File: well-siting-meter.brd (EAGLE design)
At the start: 93.8 x 65.9 mm, 55 parts, among them IC1 LM336LP, J2 7805, T1 MOSFET-NCHANNELFQP30N06L, U1 LCD-16X2NOHOLES, U2 ARDUINO_PRO_MINI, U3 EC2, U4 EC2, U5 AD623, U6 AD629, U7 MAX1771

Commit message: rev B build
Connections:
- net RSW: now also U2.10; no longer U2.A5
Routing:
- net RSW: track 33.9 -> 54.7 mm
- net VO: track 40.7 -> 40.1 mm
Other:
- board text added: "danwahl.net/"
- board text removed: "danwahl.github.io/"
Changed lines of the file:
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@@
 <text x="92.71" y="42.418" size="1.4224" layer="121" font="vector" ratio="10" rot="R90">well-siting-meter</text>
 <text x="87.63" y="40.64" size="0.8128" layer="121" font="vector" ratio="10" rot="R90">v2</text>
-<text x="92.71" y="30.48" size="0.8128" layer="121" font="vector" ratio="10" rot="R90">danwahl.github.io/</text>
+<text x="92.71" y="34.29" size="0.8128" layer="121" font="vector" ratio="10" rot="R90">danwahl.net/</text>
 <text x="87.63" y="64.77" size="1.016" layer="121" font="vector" ratio="10" align="center">BATT</text>
 <text x="71.374" y="64.77" size="1.016" layer="121" font="vector" ratio="10" align="center">GND</text>
@@
 </element>
 <element name="C1" library="SparkFun-Passives" package="CPOL-RADIAL-1000UF-25V" value="100uF" x="59.69" y="26.67" smashed="yes" rot="R180">
-<attribute name="NAME" x="60.452" y="25.019" size="0.8128" layer="25" font="vector" rot="R180"/>
+<attribute name="NAME" x="65.532" y="31.369" size="0.8128" layer="25" font="vector" rot="R180"/>
 <attribute name="PN" value="1572-1306-ND" x="59.69" y="26.67" size="1.778" layer="27" rot="R180" display="off"/>
 <attribute name="VALUE" x="62.357" y="29.972" size="0.8128" layer="27" font="vector" rot="R180"/>
@@
 <attribute name="NAME" x="48.26" y="22.098" size="0.8128" layer="25" font="vector" rot="R90"/>
 <attribute name="PN" value="BC2665CT-ND" x="49.53" y="24.13" size="1.778" layer="27" rot="R90" display="off"/>
-<attribute name="VALUE" x="51.562" y="20.574" size="0.8128" layer="27" font="vector" rot="R90"/>
+<attribute name="VALUE" x="51.562" y="24.384" size="0.8128" layer="27" font="vector" rot="R90"/>
 </element>
 <element name="C3" library="SparkFun-Passives" package="CAP-PTH-5MM" value="0.1uf" x="41.91" y="13.97" smashed="yes" rot="R180">
-<attribute name="NAME" x="40.132" y="12.7" size="0.8128" layer="25" font="vector" rot="R180"/>
+<attribute name="NAME" x="43.942" y="16.002" size="0.8128" layer="25" font="vector" rot="R180"/>
 <attribute name="PN" value="BC2665CT-ND" x="41.91" y="13.97" size="1.778" layer="27" rot="R180" display="off"/>
 <attribute name="VALUE" x="40.386" y="16.002" size="0.8128" layer="27" font="vector" rot="R180"/>
@@
 </element>
 <element name="R9" library="SparkFun-Passives" package="AXIAL-0.4" value="1M" x="34.29" y="8.89" smashed="yes" rot="R90">
-<attribute name="NAME" x="32.385" y="5.715" size="0.8128" layer="25" font="vector" ratio="10" rot="R90"/>
+<attribute name="NAME" x="32.385" y="10.795" size="0.8128" layer="25" font="vector" ratio="10" rot="R90"/>
 <attribute name="PN" value="1.00MXBK-ND" x="34.29" y="8.89" size="1.778" layer="27" rot="R90" display="off"/>
 <attribute name="VALUE" x="34.671" y="6.604" size="0.8128" layer="27" font="vector" ratio="10" rot="R90"/>
 </element>
 <element name="C6" library="SparkFun-Passives" package="CAP-PTH-5MM" value="0.1uf" x="30.48" y="6.35" smashed="yes" rot="R90">
-<attribute name="NAME" x="29.21" y="6.858" size="0.8128" layer="25" font="vector" rot="R90"/>
+<attribute name="NAME" x="29.21" y="4.318" size="0.8128" layer="25" font="vector" rot="R90"/>
 <attribute name="PN" value="445-173449-1-ND" x="30.48" y="6.35" size="1.778" layer="27" rot="R90" display="off"/>
-<attribute name="VALUE" x="32.512" y="6.604" size="0.8128" layer="27" font="vector" rot="R90"/>
+<attribute name="VALUE" x="32.004" y="5.334" size="0.8128" layer="27" font="vector" rot="R90"/>
 </element>
 <element name="C4" library="SparkFun-Passives" package="CPOL-RADIAL-1000UF-25V" value="4u7" x="41.91" y="6.35" smashed="yes" rot="R270">
-<attribute name="NAME" x="43.561" y="7.112" size="0.8128" layer="25" font="vector" rot="R270"/>
+<attribute name="NAME" x="36.703" y="11.684" size="0.8128" layer="25" font="vector" rot="R270"/>
 <attribute name="PN" value="399-6091-ND" x="41.91" y="6.35" size="1.778" layer="27" rot="R270" display="off"/>
 <attribute name="VALUE" x="45.466" y="7.493" size="0.8128" layer="27" font="vector" rot="R270"/>
@@
 </element>
 <element name="L1" library="misc" package="1415" value="22uH" x="74.93" y="24.13" smashed="yes" rot="R180">
-<attribute name="NAME" x="78.74" y="20.32" size="0.8128" layer="25" font="vector" rot="R180"/>
+<attribute name="NAME" x="80.01" y="31.75" size="0.8128" layer="25" font="vector" rot="R180"/>
 <attribute name="PN" value="732-7163-ND" x="74.93" y="24.13" size="1.778" layer="27" rot="R180" display="off"/>
 <attribute name="VALUE" x="78.74" y="29.21" size="0.8128" layer="27" font="vector" rot="R180"/>
@@
 <element name="IC1" library="linear" library_urn="urn:adsk.eagle:library:262" package="TO92" package3d_urn="urn:adsk.eagle:package:16416/2" value="LM336LP" x="22.86" y="53.594" smashed="yes">
 <attribute name="NAME" x="25.273" y="55.245" size="0.8128" layer="25" font="vector" ratio="10"/>
+<attribute name="PN" value="LM336Z25-ND" x="22.86" y="53.594" size="1.778" layer="27" display="off"/>
 <attribute name="VALUE" x="25.781" y="52.324" size="0.8128" layer="27" font="vector" ratio="10"/>
 </element>
 <element name="C11" library="SparkFun-Passives" package="CAP-PTH-5MM" value="0.1uf" x="8.89" y="53.34" smashed="yes" rot="R180">
-<attribute name="NAME" x="11.684" y="52.324" size="0.8128" layer="25" font="vector" ratio="10" rot="R180"/>
+<attribute name="NAME" x="9.144" y="54.864" size="0.8128" layer="25" font="vector" ratio="10" rot="R180"/>
 <attribute name="PN" value="BC2665CT-ND" x="8.89" y="53.34" size="0.8128" layer="27" font="vector" ratio="10" rot="R180" display="off"/>
-<attribute name="VALUE" x="9.906" y="54.864" size="0.8128" layer="27" font="vector" ratio="10" rot="R180"/>
+<attribute name="VALUE" x="12.446" y="52.324" size="0.8128" layer="27" font="vector" ratio="10" rot="R180"/>
 </element>
 </elements>
@@
 <contactref element="U1" pad="4"/>
 <contactref element="U2" pad="5"/>
-<wire x1="73.66" y1="56.134" x2="75.692" y2="54.102" width="0.3048" layer="1"/>
+<wire x1="75.438" y1="53.848" x2="73.66" y2="56.134" width="0.3048" layer="1"/>
 <wire x1="60.96" y1="54.61" x2="62.484" y2="56.134" width="0.3048" layer="1"/>
 <wire x1="62.484" y1="56.134" x2="73.66" y2="56.134" width="0.3048" layer="1"/>
-<wire x1="75.692" y1="54.102" x2="75.692" y2="38.872" width="0.3048" layer="1"/>
-<wire x1="75.692" y1="38.872" x2="71.37" y2="34.55" width="0.3048" layer="1"/>
+<wire x1="71.37" y1="34.55" x2="75.438" y2="38.618" width="0.3048" layer="1"/>
+<wire x1="75.438" y1="38.618" x2="75.438" y2="53.848" width="0.3048" layer="1"/>
 </signal>
 <signal name="E">
@@
 <contactref element="U1" pad="3"/>
 <contactref element="U2" pad="6"/>
-<wire x1="74.168" y1="56.642" x2="76.45" y2="54.36" width="0.3048" layer="1"/>
+<wire x1="75.942" y1="54.36" x2="74.168" y2="56.642" width="0.3048" layer="1"/>
 <wire x1="58.42" y1="54.61" x2="60.452" y2="56.642" width="0.3048" layer="1"/>
 <wire x1="60.452" y1="56.642" x2="74.168" y2="56.642" width="0.3048" layer="1"/>
-<wire x1="76.45" y1="54.36" x2="76.45" y2="37.09" width="0.3048" layer="1"/>
-<wire x1="76.45" y1="37.09" x2="73.91" y2="34.55" width="0.3048" layer="1"/>
+<wire x1="73.91" y1="34.55" x2="75.942" y2="36.582" width="0.3048" layer="1"/>
+<wire x1="75.942" y1="36.582" x2="75.942" y2="54.36" width="0.3048" layer="1"/>
 </signal>
 <signal name="N$3">
@@
 <polygon width="0.3048" layer="1">
 <vertex x="55.88" y="13.97"/>
-<vertex x="66.04" y="13.97"/>
-<vertex x="66.04" y="5.08"/>
-<vertex x="55.88" y="5.08"/>
-<vertex x="55.88" y="-1.27"/>
-<vertex x="70.358" y="-1.27"/>
-<vertex x="70.358" y="25.654"/>
-<vertex x="66.04" y="25.654"/>
-<vertex x="66.04" y="16.51"/>
+<vertex x="66.802" y="13.97"/>
+<vertex x="66.802" y="5.08"/>
+<vertex x="62.23" y="5.08"/>
+<vertex x="62.23" y="-1.27"/>
+<vertex x="69.85" y="-1.27"/>
+<vertex x="69.85" y="7.874"/>
+<vertex x="70.612" y="7.874"/>
+<vertex x="70.612" y="25.654"/>
+<vertex x="66.802" y="25.654"/>
+<vertex x="66.802" y="16.51"/>
 <vertex x="55.88" y="16.51"/>
 </polygon>
@@
 <vertex x="55.88" y="16.51"/>
 <vertex x="55.88" y="20.574"/>
-<vertex x="66.04" y="20.574"/>
-<vertex x="66.04" y="16.51"/>
+<vertex x="66.802" y="20.574"/>
+<vertex x="66.802" y="16.51"/>
 </polygon>
 </signal>
@@
 <polygon width="0.3048" layer="1" rank="3">
 <vertex x="55.88" y="13.97"/>
-<vertex x="55.88" y="5.08"/>
-<vertex x="66.04" y="5.08"/>
-<vertex x="66.04" y="13.97"/>
+<vertex x="55.88" y="8.89"/>
+<vertex x="62.23" y="8.89"/>
+<vertex x="62.23" y="5.08"/>
+<vertex x="66.802" y="5.08"/>
+<vertex x="66.802" y="13.97"/>
 </polygon>
 </signal>
@@
 <signal name="RSW">
 <contactref element="R6" pad="P$1"/>
-<contactref element="U2" pad="A5"/>
 <wire x1="67.564" y1="30.226" x2="74.93" y2="22.86" width="0.3048" layer="16"/>
 <wire x1="74.93" y1="22.86" x2="74.93" y2="13.97" width="0.3048" layer="16"/>
-<wire x1="67.564" y1="35.306" x2="64.77" y2="38.1" width="0.3048" layer="16"/>
+<wire x1="64.77" y1="38.1" x2="67.564" y2="35.306" width="0.3048" layer="16"/>
 <wire x1="67.564" y1="35.306" x2="67.564" y2="30.226" width="0.3048" layer="16"/>
-<wire x1="64.77" y1="40.64" x2="63.1825" y2="42.2275" width="0.3048" layer="16"/>
-<wire x1="63.1825" y1="42.2275" x2="62.38875" y2="42.2275" width="0.3048" layer="16"/>
-<wire x1="64.77" y1="38.1" x2="64.77" y2="40.64" width="0.3048" layer="16"/>
+<contactref element="U2" pad="10"/>
+<wire x1="48.26" y1="54.61" x2="58.42" y2="44.45" width="0.3048" layer="16"/>
+<wire x1="58.42" y1="44.45" x2="63.5" y2="44.45" width="0.3048" layer="16"/>
+<wire x1="63.5" y1="44.45" x2="64.77" y2="43.18" width="0.3048" layer="16"/>
+<wire x1="64.77" y1="43.18" x2="64.77" y2="38.1" width="0.3048" layer="16"/>
 </signal>
 <signal name="FUSE">

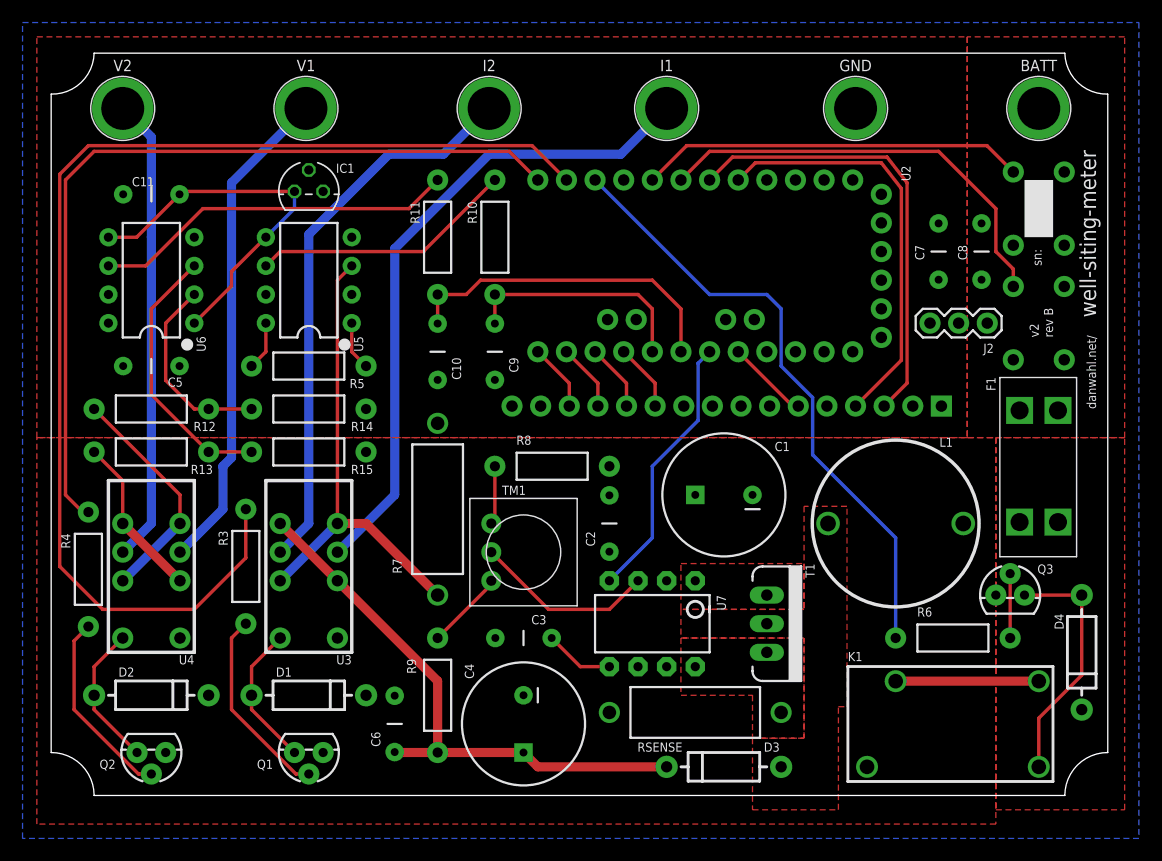
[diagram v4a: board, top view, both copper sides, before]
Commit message: rev C initial commit, modifying vref and voltage input resistors
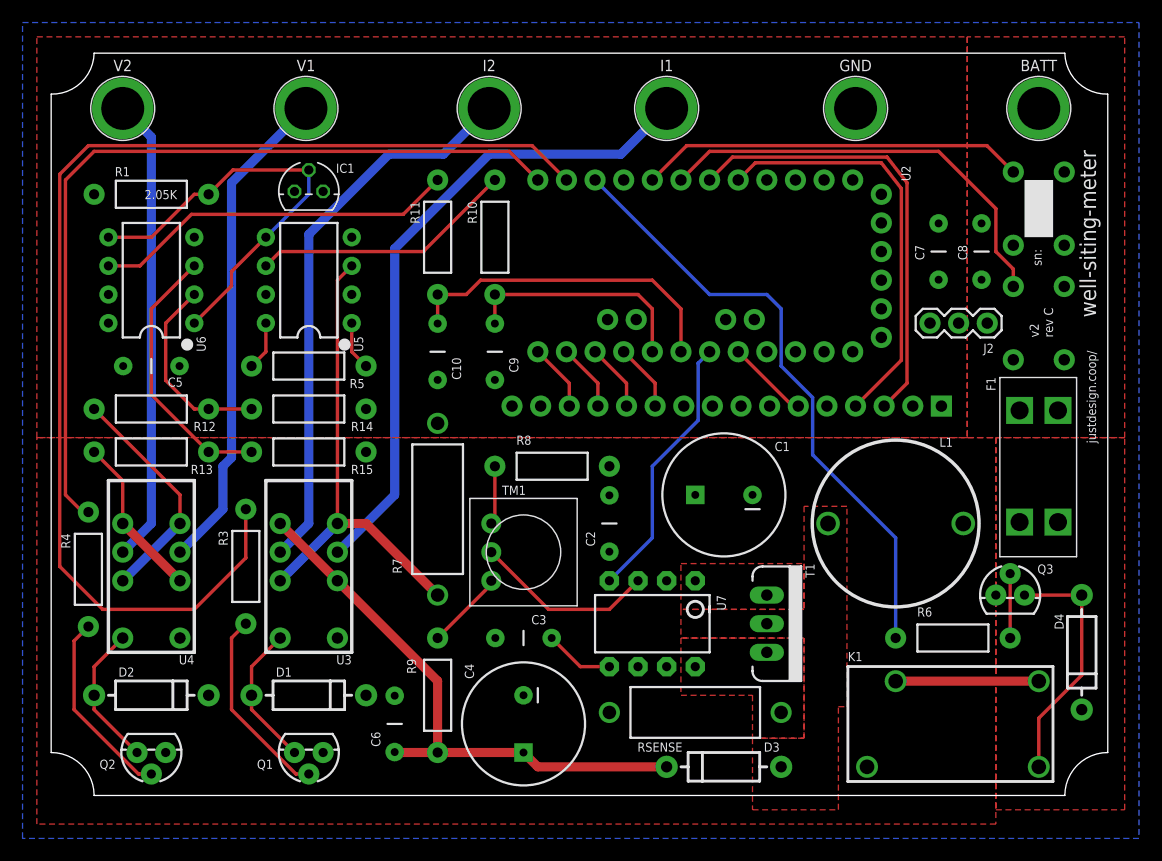
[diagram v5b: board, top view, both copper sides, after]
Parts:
- removed C11: 0.1uf, SparkFun-Passives:CAP-PTH-5MM
- added R1: 2.05K, SparkFun-Passives:AXIAL-0.4
- R12, R13: value 10K -> 44.2K
- R14, R15: value 44.2K -> 10K
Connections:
- net 5V: now also R1.P$2; no longer IC1.2
- net GND: no longer C11.2
- net VREF: now also IC1.2, R1.P$1; no longer C11.1, IC1.1
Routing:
- net VREF: track 33.6 -> 38.0 mm
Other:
- board text added: "justdesign.coop/"
- board text added: "rev C"
- board text removed: "danwahl.net/"
- board text removed: "rev B"
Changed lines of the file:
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@@
 <?xml version="1.0" encoding="utf-8"?>
 <!DOCTYPE eagle SYSTEM "eagle.dtd">
-<eagle version="9.0.0">
+<eagle version="9.1.0">
 <drawing>
 <settings>
@@
 <text x="92.71" y="42.418" size="1.4224" layer="121" font="vector" ratio="10" rot="R90">well-siting-meter</text>
 <text x="87.63" y="40.64" size="0.8128" layer="121" font="vector" ratio="10" rot="R90">v2</text>
-<text x="92.71" y="34.29" size="0.8128" layer="121" font="vector" ratio="10" rot="R90">danwahl.net/</text>
+<text x="92.71" y="31.242" size="0.8128" layer="121" font="vector" ratio="10" rot="R90">justdesign.coop/</text>
 <text x="87.63" y="64.77" size="1.016" layer="121" font="vector" ratio="10" align="center">BATT</text>
 <text x="71.374" y="64.77" size="1.016" layer="121" font="vector" ratio="10" align="center">GND</text>
@@
 <text x="22.606" y="64.77" size="1.016" layer="122" font="vector" ratio="10" rot="MR0" align="center">V1</text>
 <text x="6.35" y="64.77" size="1.016" layer="122" font="vector" ratio="10" rot="MR0" align="center">V2</text>
-<text x="88.9" y="40.64" size="0.8128" layer="121" font="vector" ratio="10" rot="R90">rev B</text>
+<text x="88.9" y="40.64" size="0.8128" layer="121" font="vector" ratio="10" rot="R90">rev C</text>
 <text x="87.884" y="46.99" size="0.8128" layer="121" font="vector" ratio="10" rot="R90">sn:</text>
 <rectangle x1="86.36" y1="49.53" x2="88.9" y2="54.61" layer="121"/>
@@
 <param name="checkStop" value="0"/>
 <param name="checkValues" value="0"/>
+<param name="checkNames" value="1"/>
+<param name="checkWireStubs" value="1"/>
+<param name="checkPolygonWidth" value="0"/>
 <param name="useDiameter" value="13"/>
 <param name="maxErrors" value="50"/>
@@
 <attribute name="VALUE" x="80.338" y="6.077" size="1.27" layer="27" rot="R180" align="center"/>
 </element>
-<element name="R12" library="SparkFun-Passives" package="AXIAL-0.4" value="10K" x="8.89" y="34.29" smashed="yes">
+<element name="R12" library="SparkFun-Passives" package="AXIAL-0.4" value="44.2K" x="8.89" y="34.29" smashed="yes">
 <attribute name="NAME" x="14.605" y="33.147" size="0.8128" layer="25" font="vector" ratio="10" align="top-right"/>
-<attribute name="PN" value="10.0KXBK-ND" x="8.89" y="34.29" size="1.778" layer="27" display="off"/>
+<attribute name="PN" value="44.2KXBK-ND" x="8.89" y="34.29" size="1.778" layer="27" display="off"/>
 <attribute name="VALUE" x="6.604" y="33.909" size="0.8128" layer="27" font="vector" ratio="10"/>
 </element>
-<element name="R13" library="SparkFun-Passives" package="AXIAL-0.4" value="10K" x="8.89" y="30.48" smashed="yes">
+<element name="R13" library="SparkFun-Passives" package="AXIAL-0.4" value="44.2K" x="8.89" y="30.48" smashed="yes">
 <attribute name="NAME" x="14.351" y="29.337" size="0.8128" layer="25" font="vector" ratio="10" align="top-right"/>
-<attribute name="PN" value="10.0KXBK-ND" x="8.89" y="30.48" size="1.778" layer="27" display="off"/>
+<attribute name="PN" value="44.2KXBK-ND" x="8.89" y="30.48" size="1.778" layer="27" display="off"/>
 <attribute name="VALUE" x="6.604" y="30.099" size="0.8128" layer="27" font="vector" ratio="10"/>
 </element>
-<element name="R14" library="SparkFun-Passives" package="AXIAL-0.4" value="44.2K" x="22.86" y="34.29" smashed="yes" rot="R180">
+<element name="R14" library="SparkFun-Passives" package="AXIAL-0.4" value="10K" x="22.86" y="34.29" smashed="yes" rot="R180">
 <attribute name="NAME" x="28.575" y="33.147" size="0.8128" layer="25" font="vector" rot="R180"/>
-<attribute name="PN" value="44.2KXBK-ND" x="22.86" y="34.29" size="1.778" layer="27" rot="R180" display="off"/>
+<attribute name="PN" value="10.0KXBK-ND" x="22.86" y="34.29" size="1.778" layer="27" rot="R180" display="off"/>
 <attribute name="VALUE" x="25.146" y="34.671" size="0.8128" layer="27" font="vector" rot="R180"/>
 </element>
-<element name="R15" library="SparkFun-Passives" package="AXIAL-0.4" value="44.2K" x="22.86" y="30.48" smashed="yes" rot="R180">
+<element name="R15" library="SparkFun-Passives" package="AXIAL-0.4" value="10K" x="22.86" y="30.48" smashed="yes" rot="R180">
 <attribute name="NAME" x="28.575" y="29.337" size="0.8128" layer="25" font="vector" rot="R180"/>
-<attribute name="PN" value="44.2KXBK-ND" x="22.86" y="30.48" size="1.778" layer="27" rot="R180" display="off"/>
+<attribute name="PN" value="10.0KXBK-ND" x="22.86" y="30.48" size="1.778" layer="27" rot="R180" display="off"/>
 <attribute name="VALUE" x="25.146" y="30.861" size="0.8128" layer="27" font="vector" rot="R180"/>
 </element>
@@
 <attribute name="VALUE" x="25.781" y="52.324" size="0.8128" layer="27" font="vector" ratio="10"/>
 </element>
-<element name="C11" library="SparkFun-Passives" package="CAP-PTH-5MM" value="0.1uf" x="8.89" y="53.34" smashed="yes" rot="R180">
-<attribute name="NAME" x="9.144" y="54.864" size="0.8128" layer="25" font="vector" ratio="10" rot="R180"/>
-<attribute name="PN" value="BC2665CT-ND" x="8.89" y="53.34" size="0.8128" layer="27" font="vector" ratio="10" rot="R180" display="off"/>
-<attribute name="VALUE" x="12.446" y="52.324" size="0.8128" layer="27" font="vector" ratio="10" rot="R180"/>
+<element name="R1" library="SparkFun-Passives" package="AXIAL-0.4" value="2.05K" x="8.89" y="53.34" smashed="yes" rot="R180">
+<attribute name="NAME" x="6.985" y="55.753" size="0.8128" layer="25" font="vector" ratio="15" rot="R180"/>
+<attribute name="PN" value="2.05KXBK-ND" x="8.89" y="53.34" size="1.778" layer="27" rot="R180" display="off"/>
+<attribute name="VALUE" x="11.176" y="53.721" size="0.8128" layer="21" font="vector" ratio="15" rot="R180"/>
 </element>
 </elements>
@@
 <contactref element="C5" pad="2"/>
 <contactref element="IC1" pad="3"/>
-<contactref element="C11" pad="2"/>
 </signal>
 <signal name="5V">
@@
 </polygon>
 <contactref element="C5" pad="1"/>
-<contactref element="IC1" pad="2"/>
+<contactref element="R1" pad="P$2"/>
 </signal>
 <signal name="N$1">
@@
 <wire x1="16.002" y1="46.482" x2="16.002" y2="45.212" width="0.3048" layer="1"/>
 <wire x1="16.002" y1="45.212" x2="12.7" y2="41.91" width="0.3048" layer="1"/>
-<contactref element="IC1" pad="1"/>
-<wire x1="19.05" y1="49.53" x2="21.59" y2="52.07" width="0.3048" layer="16"/>
-<wire x1="21.59" y1="52.07" x2="21.59" y2="53.594" width="0.3048" layer="16"/>
-<contactref element="C11" pad="1"/>
-<wire x1="11.39" y1="53.34" x2="7.58" y2="49.53" width="0.3048" layer="1"/>
-<wire x1="7.58" y1="49.53" x2="5.08" y2="49.53" width="0.3048" layer="1"/>
-<wire x1="11.39" y1="53.34" x2="11.644" y2="53.594" width="0.3048" layer="1"/>
-<wire x1="11.644" y1="53.594" x2="21.59" y2="53.594" width="0.3048" layer="1"/>
+<contactref element="R1" pad="P$1"/>
+<contactref element="IC1" pad="2"/>
+<wire x1="8.89" y1="49.53" x2="12.7" y2="53.34" width="0.3048" layer="1"/>
+<wire x1="12.7" y1="53.34" x2="13.97" y2="53.34" width="0.3048" layer="1"/>
+<wire x1="5.08" y1="49.53" x2="8.89" y2="49.53" width="0.3048" layer="1"/>
+<wire x1="13.97" y1="53.34" x2="16.129" y2="55.499" width="0.3048" layer="1"/>
+<wire x1="16.129" y1="55.499" x2="22.86" y2="55.499" width="0.3048" layer="1"/>
+<wire x1="22.86" y1="53.34" x2="22.86" y2="55.499" width="0.3048" layer="16"/>
+<wire x1="19.05" y1="49.53" x2="22.86" y2="53.34" width="0.3048" layer="16"/>
 </signal>
 <signal name="V_BATT">
@@
 <contactref element="U6" pad="6"/>
 <contactref element="R11" pad="P$1"/>
-<wire x1="34.29" y1="54.61" x2="31.75" y2="52.07" width="0.3048" layer="1"/>
-<wire x1="13.462" y1="52.07" x2="8.382" y2="46.99" width="0.3048" layer="1"/>
-<wire x1="8.382" y1="46.99" x2="5.08" y2="46.99" width="0.3048" layer="1"/>
-<wire x1="31.75" y1="52.07" x2="13.462" y2="52.07" width="0.3048" layer="1"/>
+<wire x1="34.29" y1="54.61" x2="31.242" y2="51.562" width="0.3048" layer="1"/>
+<wire x1="12.446" y1="51.562" x2="7.874" y2="46.99" width="0.3048" layer="1"/>
+<wire x1="7.874" y1="46.99" x2="5.08" y2="46.99" width="0.3048" layer="1"/>
+<wire x1="31.242" y1="51.562" x2="12.446" y2="51.562" width="0.3048" layer="1"/>
 </signal>
 <signal name="BATT">
@@
 </signal>
 </signals>
+<mfgpreviewcolors>
+<mfgpreviewcolor name="soldermaskcolor" color="0xC8008000"/>
+<mfgpreviewcolor name="silkscreencolor" color="0xFFFEFEFE"/>
+<mfgpreviewcolor name="backgroundcolor" color="0xFF282828"/>
+<mfgpreviewcolor name="coppercolor" color="0xFFFFBF00"/>
+<mfgpreviewcolor name="substratecolor" color="0xFF786E46"/>
+</mfgpreviewcolors>
 </board>
 </drawing>
